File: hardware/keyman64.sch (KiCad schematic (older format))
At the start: 36 parts, among them IC1 ATMEGA1284P-PU, J1 POWER, P1 SERIAL, P2 COMPUTER, P3 KEYBOARD, P4 CONTROL, P6 USB, SW1 RESET, SW2 BOOT, U1 7400, U2 7660, U3 4520, U4 4051, U5 4051, U6 CD74HC22106/MT8808, X1 16MHz

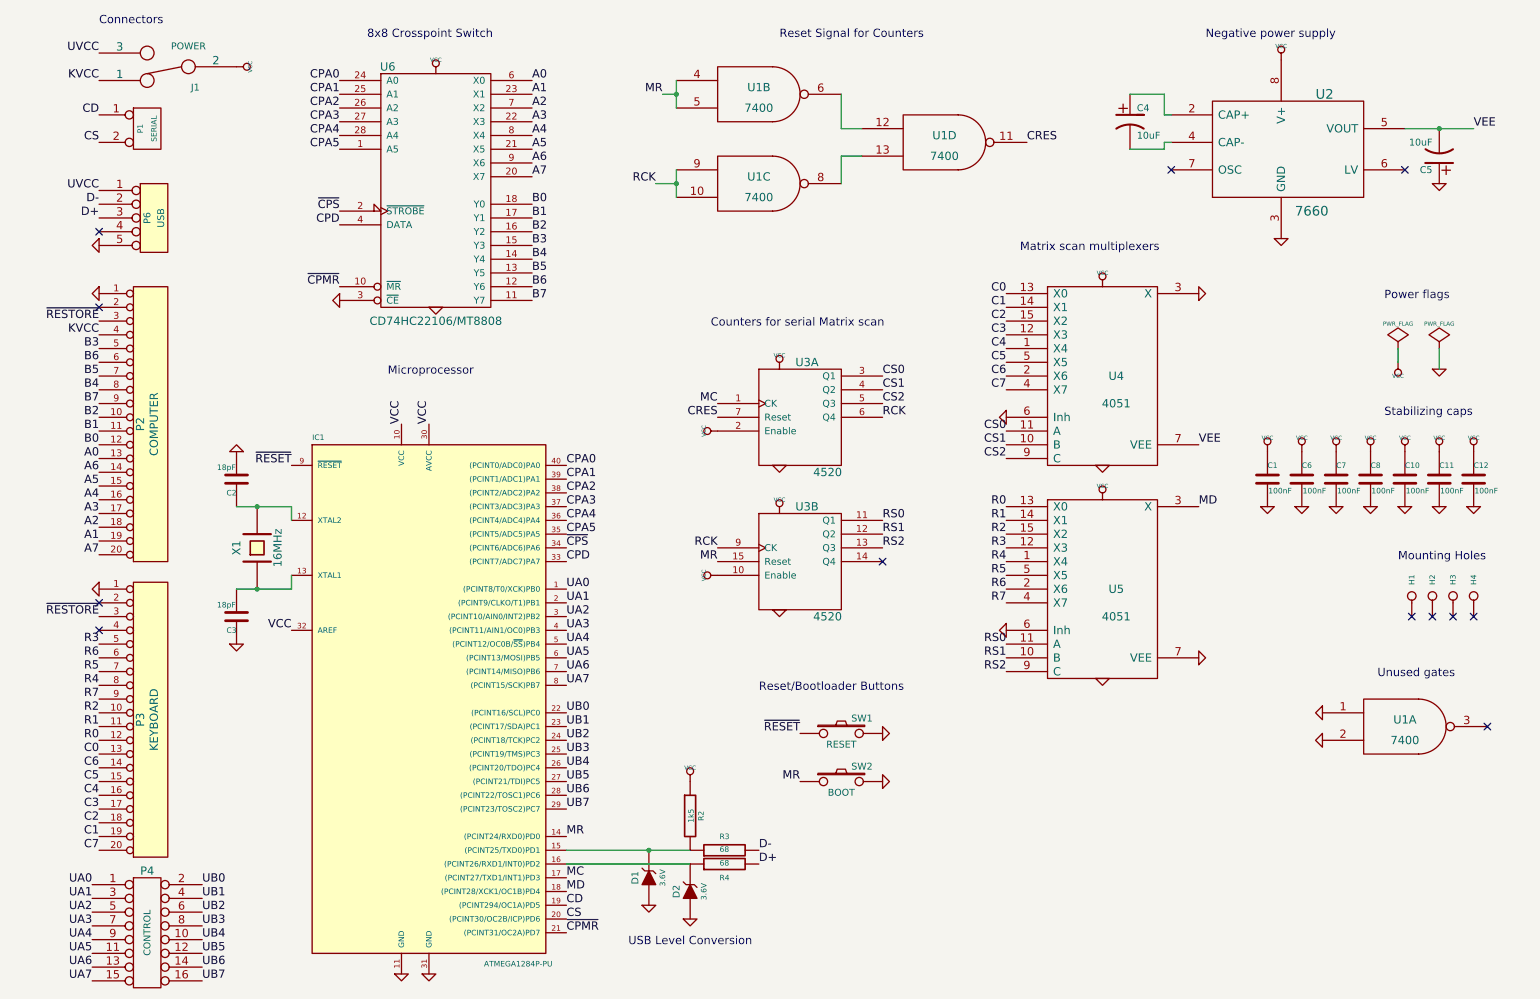
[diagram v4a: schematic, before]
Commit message: Hardware: Reassigned/cleaned up component references
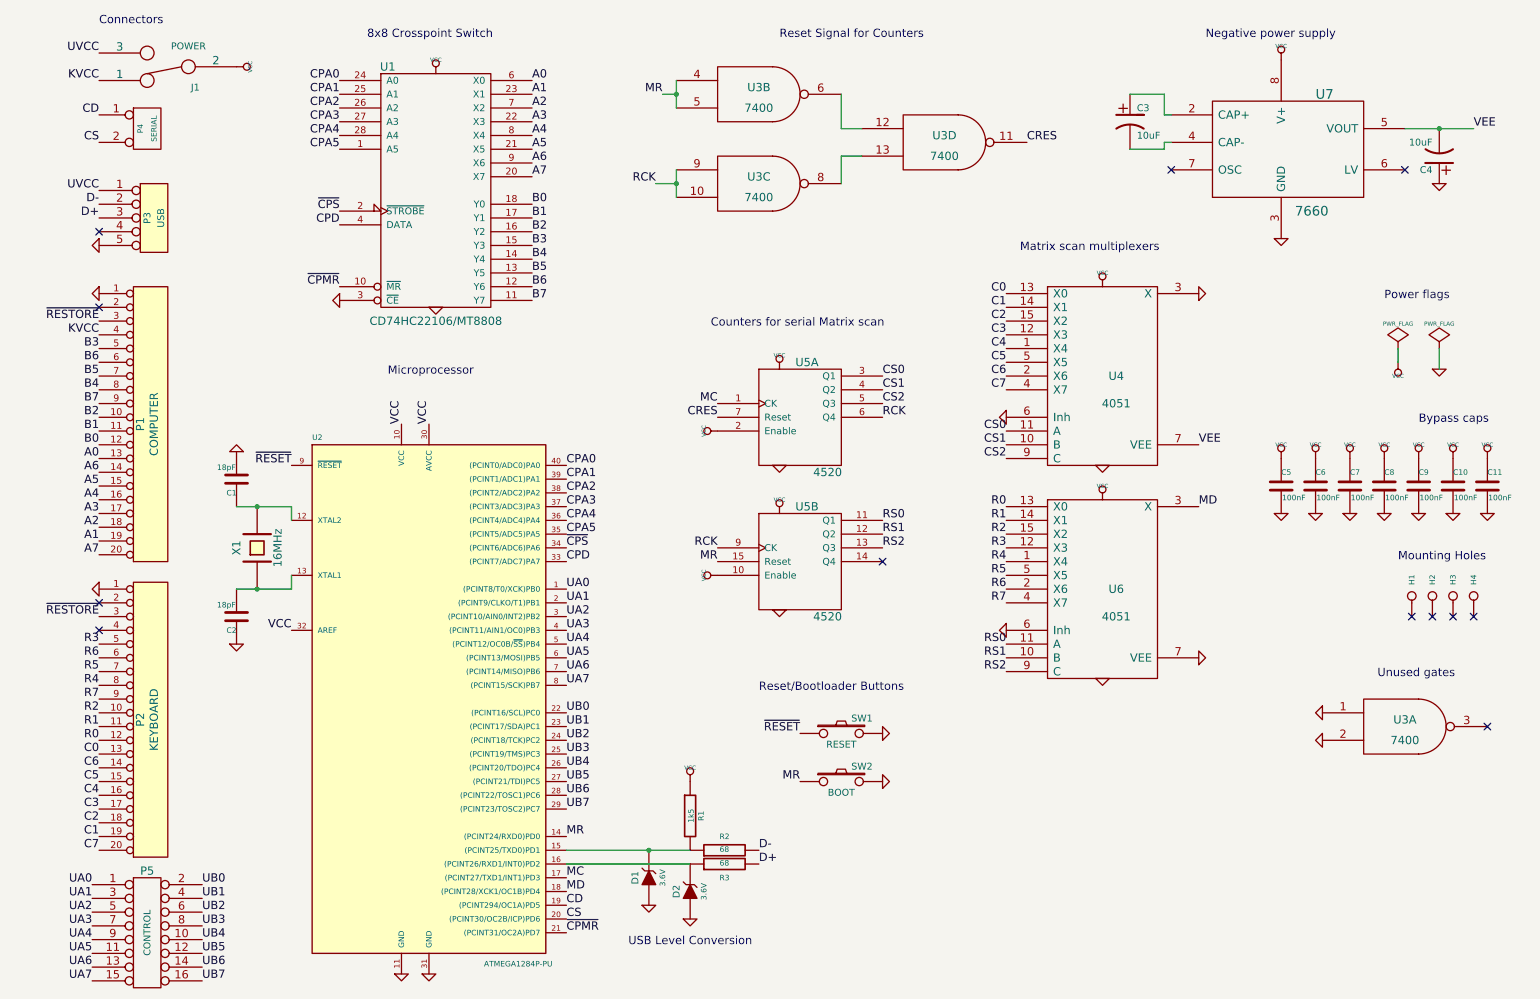
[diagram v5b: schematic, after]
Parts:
- renumbered C2 to C1, C7 to C10, C8 to C11, C3 to C2, C4 to C3, C5 to C4, C10 to C5, C11 to C6, C12 to C7, C1 to C8, C6 to C9, P2 to P1, P3 to P2, P6 to P3, P1 to P4, P4 to P5, R2 to R1, R3 to R2, R4 to R3, U6 to U1, IC1 to U2, U1 to U3, U3 to U5, U5 to U6, U2 to U7
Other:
- note added: "Bypass caps"
- note removed: "Stabilizing caps"
- moved on the sheet: C10, C11, C5, C6, C7, C8, C9

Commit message: Hardware: Removed all legacy components in schematics
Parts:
- C1, C10, C11, C2, C5, C6, C7, C8, C9: symbol C-RESCUE-keyman64 -> C
- C3, C4: symbol CP1-RESCUE-keyman64 -> CP1
- D1, D2: symbol ZENER-RESCUE-keyman64 -> ZENER
- R1, R2, R3: symbol R-RESCUE-keyman64 -> R
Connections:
- net GND: now also D1.2 (A), D2.2 (A); no longer D1.1 (A), D2.1 (A)
- net at R1.2, R2.1, U2.15 ((PCINT25/TXD0)PD1): now also D1.1 (K); no longer D1.2 (K)
- net at R3.1, U2.16 ((PCINT26/RXD1/INT0)PD2): now also D2.1 (K); no longer D2.2 (K)
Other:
- moved on the sheet: C1, C2, R2, R3

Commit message: Hardware: Increased mounting hole size to 4mm
This was self-adhesive pcb holders like reichelts AHS 4,8 may be used
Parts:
- H1, H2, H3, H4: footprint Mounting_Holes:MountingHole_3mm -> Mounting_Holes:MountingHole_4mm
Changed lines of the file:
@@
 F 0 "H1" H 10530 4850 40  0000 L CNN
 F 1 "CONN_1" H 10450 4905 30  0001 C CNN
-F 2 "Mounting_Holes:MountingHole_3mm" H 10450 4850 60  0001 C CNN
+F 2 "Mounting_Holes:MountingHole_4mm" H 10450 4850 60  0001 C CNN
 F 3 "" H 10450 4850 60  0000 C CNN
 	1    10450 4850
@@
 F 0 "H2" H 10680 4850 40  0000 L CNN
 F 1 "CONN_1" H 10600 4905 30  0001 C CNN
-F 2 "Mounting_Holes:MountingHole_3mm" H 10600 4850 60  0001 C CNN
+F 2 "Mounting_Holes:MountingHole_4mm" H 10600 4850 60  0001 C CNN
 F 3 "" H 10600 4850 60  0000 C CNN
 	1    10600 4850
@@
 F 0 "H3" H 10830 4850 40  0000 L CNN
 F 1 "CONN_1" H 10750 4905 30  0001 C CNN
-F 2 "Mounting_Holes:MountingHole_3mm" H 10750 4850 60  0001 C CNN
+F 2 "Mounting_Holes:MountingHole_4mm" H 10750 4850 60  0001 C CNN
 F 3 "" H 10750 4850 60  0000 C CNN
 	1    10750 4850
@@
 F 0 "H4" H 10980 4850 40  0000 L CNN
 F 1 "CONN_1" H 10900 4905 30  0001 C CNN
-F 2 "Mounting_Holes:MountingHole_3mm" H 10900 4850 60  0001 C CNN
+F 2 "Mounting_Holes:MountingHole_4mm" H 10900 4850 60  0001 C CNN
 F 3 "" H 10900 4850 60  0000 C CNN
 	1    10900 4850

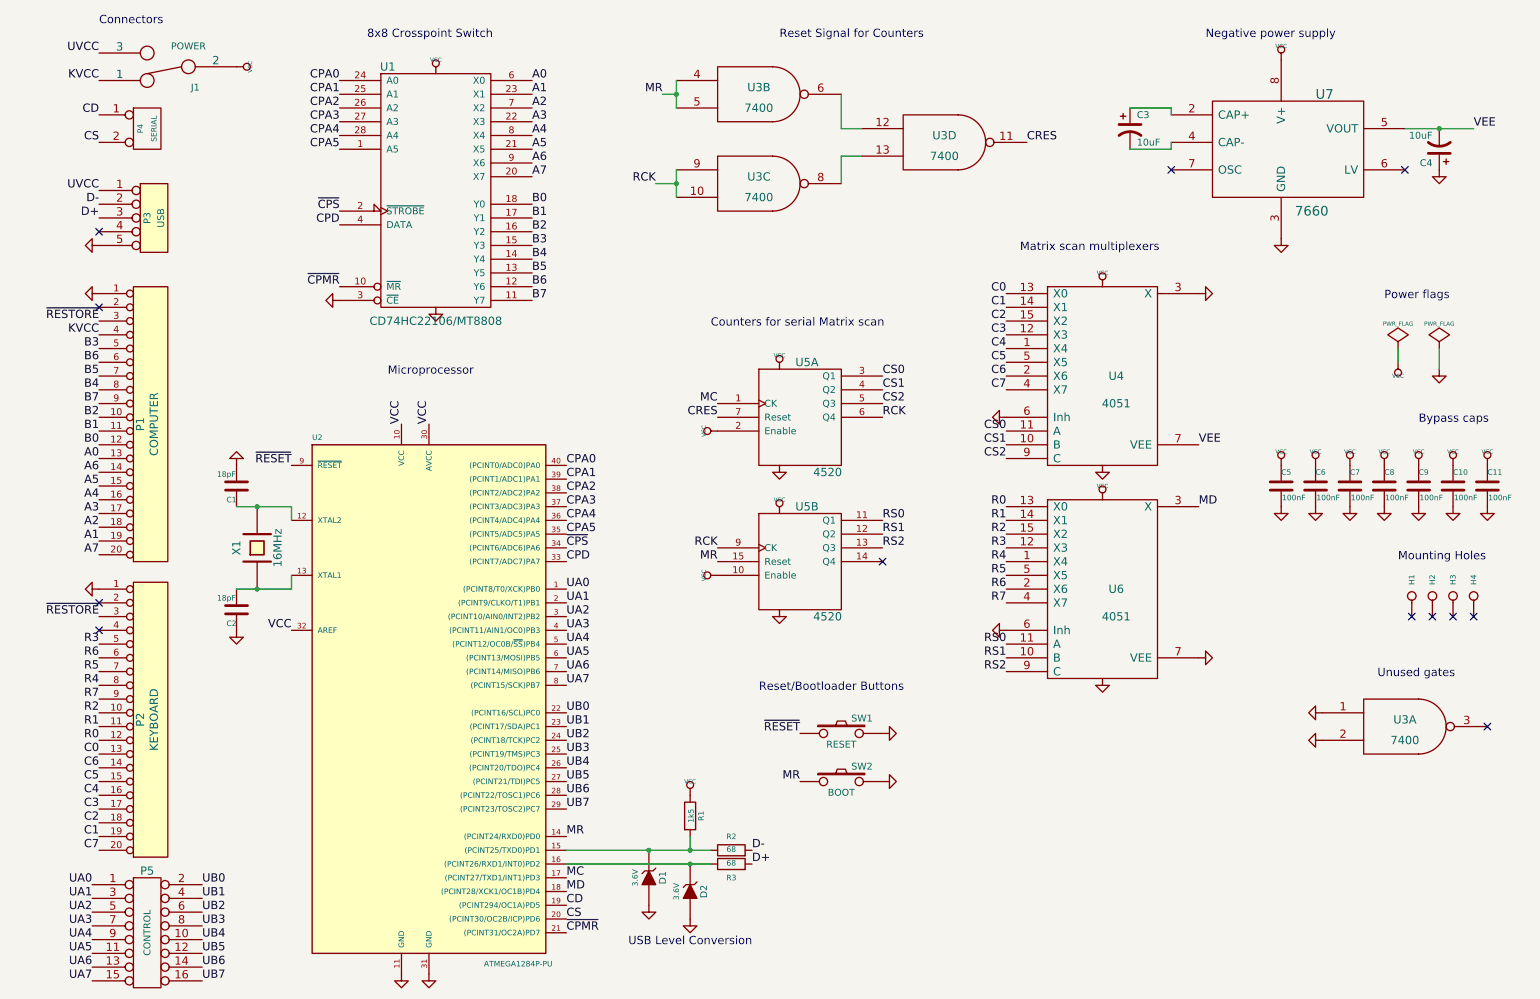
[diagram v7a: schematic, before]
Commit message: Hardware: Removed useless 7660, added alternative plcc-socket for mt8808
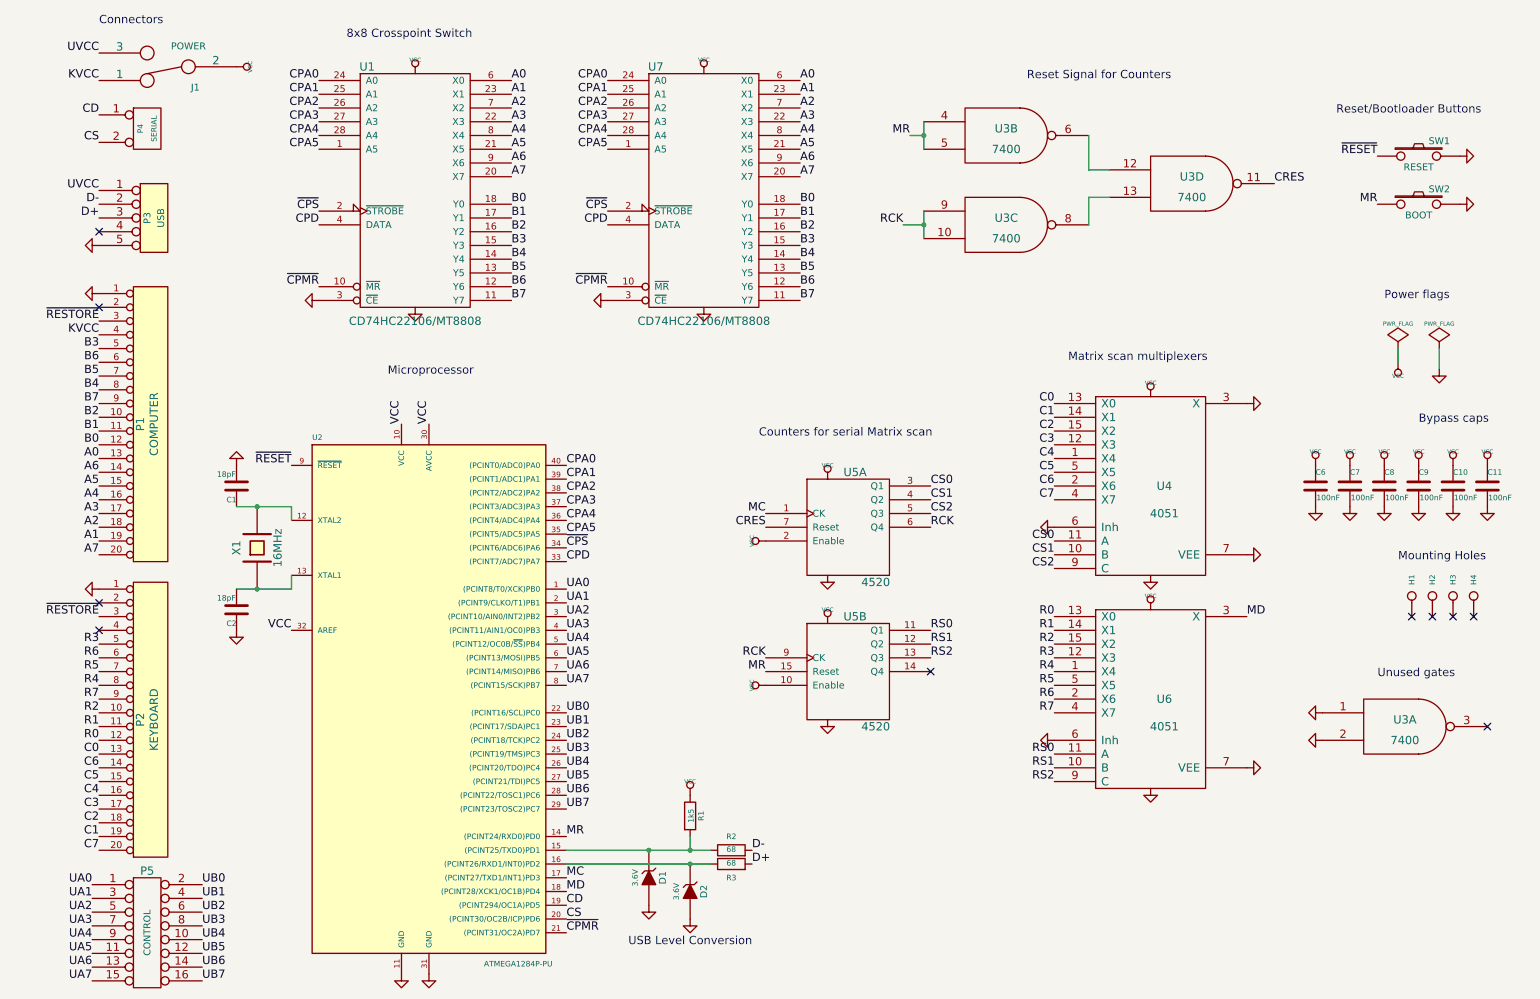
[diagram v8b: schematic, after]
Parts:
- removed C3, C4: 10uF, Capacitors_ThroughHole:C_Disc_D3_P2.5, symbol CP1
- removed C5: 100nF, Capacitors_ThroughHole:C_Disc_D3_P2.5, symbol C
- removed U7: 7660, Sockets_DIP:DIP-8__300, symbol ICL7660
- added U7: CD74HC22106/MT8808, Sockets:PLCC28, symbol CD74HC22106
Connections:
- net VEE is gone; now on net GND: U4.7 (VEE)
- net A0: now also U7.6 (X0)
- net A1: now also U7.23 (X1)
- net A2: now also U7.7 (X2)
- net A3: now also U7.22 (X3)
- net A4: now also U7.8 (X4)
- net A5: now also U7.21 (X5)
- net A6: now also U7.9 (X6)
- net A7: now also U7.20 (X7)
- net B0: now also U7.18 (Y0)
- net B1: now also U7.17 (Y1)
- net B2: now also U7.16 (Y2)
- net B3: now also U7.15 (Y3)
- net B4: now also U7.14 (Y4)
- net B5: now also U7.13 (Y5)
- net B6: now also U7.12 (Y6)
- net B7: now also U7.11 (Y7)
- net CPA0: now also U7.24 (A0)
- net CPA1: now also U7.25 (A1)
- net CPA2: now also U7.26 (A2)
- net CPA3: now also U7.27 (A3)
- net CPA4: now also U7.28 (A4)
- net CPA5: now also U7.1 (A5)
- net CPD: now also U7.4 (DATA)
- net GND: now also U7.3 (~CE), U7.5 (VSS)
- net VCC: now also U7.19 (VDD)
- net ~CPMR: now also U7.10 (~MR)
- net ~CPS: now also U7.2 (~STROBE)
- no-connect marks 12 -> 10
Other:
- note removed: "Negative power supply"
- moved on the sheet: SW1, SW2, U1, U3B, U3C, U3D, U4, U5A, U5B, U6
